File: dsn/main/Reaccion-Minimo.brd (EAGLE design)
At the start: 68.2 x 35.5 mm, 43 parts, among them U1 ATMEGA328P_TQFP, U2 MIC5219 5V, Y1 16MHz

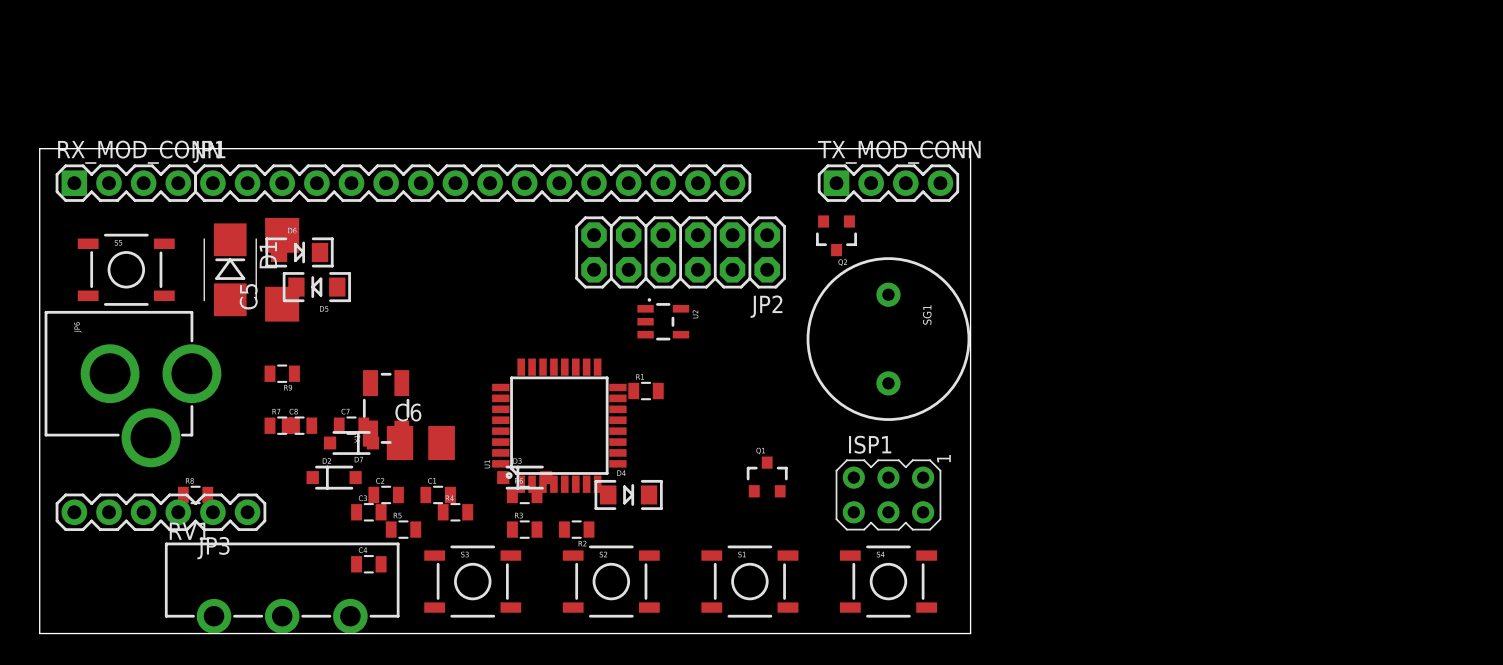
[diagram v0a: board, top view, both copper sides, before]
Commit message: Reaccion Minimo UI finished. RX send tested.
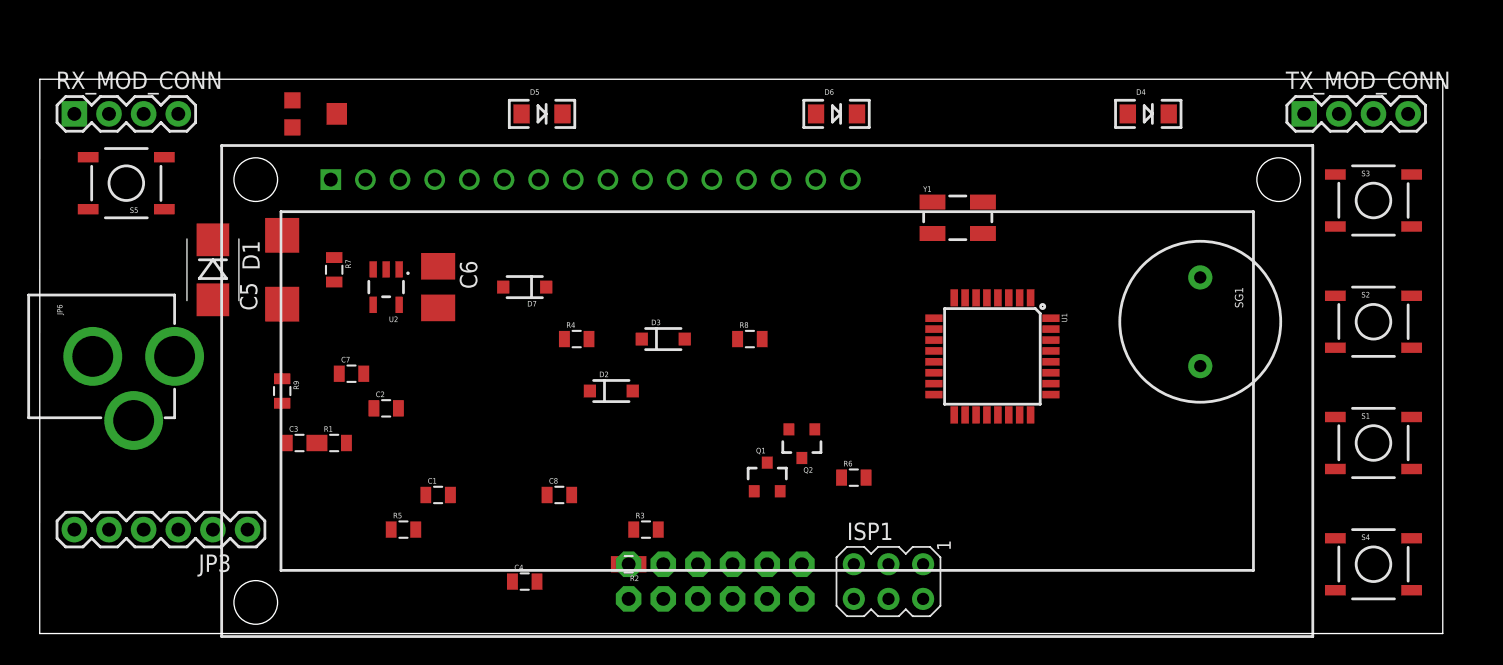
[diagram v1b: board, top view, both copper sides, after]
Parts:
- removed JP1: (no value), SparkFun-Connectors:1X16
- removed RV1: (no value), SparkFun-Electromechanical:POT_ALPHA_RV16AF-20
- added U$1: LCD-HD447803-HOLES16X2-3-HOLES, HD44780LCD:LCD-16X2-3HOLES
- added U$2: TC33, Reaccion-Minimo:TC33
- moved S3 71.7 mm to (97.8, 31.8)
- moved S2 59.0 mm to (97.8, 22.9)
- moved D4 47.2 mm to (81.3, 38.1)
- moved S1 46.8 mm to (97.8, 14.0)
- moved Y1 44.2 mm to (67.3, 30.5), turned to 0 degrees
- moved R8 42.2 mm to (52.1, 21.6)
- moved D6 40.7 mm to (58.4, 38.1)
- moved S4 35.6 mm to (97.8, 5.08)
- moved TX_MOD_CONN 34.7 mm to (92.7, 38.1)
- moved U1 32.2 mm to (69.8, 20.3), turned to 270 degrees
- moved JP2 26.2 mm to (43.2, 5.08), flipped to the bottom
- moved R6 24.2 mm to (59.7, 11.4)
- moved R1 23.2 mm to (21.6, 14.0)
- moved SG1 22.9 mm to (85.1, 22.9)
- moved D2 21.3 mm to (41.9, 17.8)
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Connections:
- net 5V: now also U$1.2, U$2.1; no longer JP1.2, RV1.3
- net D2: now also U$1.11; no longer JP1.11
- net D3: now also U$1.12; no longer JP1.12
- net D4: now also U$1.13; no longer JP1.13
- net D6: now also U$1.14; no longer JP1.14
- net D8: now also U$1.4; no longer JP1.4
- net D9: now also U$1.6; no longer JP1.6
- net GND: now also U$1.1, U$1.5, U$2.3; no longer JP1.1, JP1.5, RV1.1
- net N$6: now also U$1.15; no longer JP1.15
- net N$7: now also U$1.3, U$2.2; no longer JP1.3, RV1.2
- net N$8: now also U$1.16; no longer JP1.16
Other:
- board size 68.2 x 35.5 mm -> 102.9 x 40.6 mm

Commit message: Added Reaccion-Minimo PASTO
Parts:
- removed D4: GREEN, SparkFun-LED:LED-1206
- removed S5: SWITCH-MOMENTARY-2SMD, SparkFun-Electromechanical:TACTILE-SWITCH-SMD
- removed U$1: LCD-HD447803-HOLES16X2-3-HOLES, HD44780LCD:LCD-16X2-3HOLES
- added C9: 1uF, SparkFun-Capacitors:0805
- added LCD: LCD-HD447803-HOLES16X2-3-HOLES, HD44780LCD:LCD-16X2-3HOLES
- added RESET: SWITCH-MOMENTARY-2SMD, SparkFun-Electromechanical:TACTILE-SWITCH-SMD
- added U3: WS2811, SparkFun-LED:LED-TRICOLOR-5050-IC
- C1, C2: value (none) -> 18pF
- C3, C7: value (none) -> 1uF
- C4: value (none) -> 0.1uF
- C6: value (none) -> 100uF
- C8: value (none) -> 4.7uF
- R1, R6, R8: value (none) -> 4.7K
- R2: value (none) -> 150
- R3, R4: value (none) -> 330
- R5: value (none) -> 0
- U2: value MIC5219 5V -> lp2992aim5-5.0
- moved R2 52.7 mm to (85.1, 37.1), turned to 270 degrees
- moved R5 39.5 mm to (54.4, 35.8), turned to 90 degrees
- moved D3 35.0 mm to (12.7, 33.3), turned to 270 degrees
- moved R3 34.4 mm to (31.2, 39.4), turned to 180 degrees
- moved D2 32.2 mm to (73.7, 12.2), turned to 270 degrees
- moved C3 30.5 mm to (49.5, 12.4), turned to 90 degrees
- moved C1 28.8 mm to (57.9, 12.2), turned to 90 degrees
- moved C2 25.9 mm to (50.3, 9.40)
- moved R4 24.8 mm to (56.6, 39.4), turned to 180 degrees
- moved R1 23.5 mm to (10.2, 34.5), turned to 90 degrees
- moved Q1 23.1 mm to (61.0, 33.3), turned to 90 degrees
- moved Y1 22.9 mm to (53.6, 12.2), turned to 180 degrees
- moved C4 21.7 mm to (15.2, 11.4), turned to 90 degrees
- moved R8 21.2 mm to (71.1, 12.2), turned to 270 degrees
- moved R6 19.1 mm to (61.0, 30.5), turned to 180 degrees
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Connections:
- net 5V: now also C9.2, LCD.2, U3.3, U3.5; no longer R2.2, U$1.2
- net D2: now also LCD.11; no longer U$1.11
- net D3: now also LCD.12; no longer U$1.12
- net D4: now also LCD.13; no longer U$1.13
- net D6: now also LCD.14; no longer U$1.14
- net D8: now also LCD.4; no longer U$1.4
- net D9: now also LCD.6; no longer U$1.6
- net GND: now also C9.1, LCD.1, LCD.5, RESET.1, U3.6; no longer S5.1, U$1.1, U$1.5
- net HEARTBEAT: now also R2.2; no longer D4.C
- net N$3: now also U3.2; no longer D4.A
- net N$6: now also LCD.15; no longer U$1.15
- net N$7: now also LCD.3; no longer U$1.3
- net N$8: now also LCD.16; no longer U$1.16
- net RESET: now also RESET.3; no longer S5.3
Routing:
- net GND: track 0.00 -> 364.9 mm, vias 0 -> 14
- net 5V: track 0.00 -> 308.0 mm, vias 0 -> 8
- net VIN_RECT: track 0.00 -> 182.3 mm, vias 0 -> 4
- net RESET: track 0.00 -> 148.3 mm, vias 0 -> 2
- net RF_TX: track 0.00 -> 108.9 mm, vias 0 -> 4
- net RF_RX: track 0.00 -> 99.1 mm, vias 0 -> 4
- net BTN_BUS0: track 0.00 -> 92.4 mm, vias 0 -> 4
- net D8: track 0.00 -> 83.8 mm, vias 0 -> 6
- net BTN_BUS3: track 0.00 -> 79.9 mm, vias 0 -> 4
- net BTN_BUS2: track 0.00 -> 62.1 mm, vias 0 -> 2
- net BTN_BUS1: track 0.00 -> 62.0 mm, vias 0 -> 2
- net D9: track 0.00 -> 59.7 mm, vias 0 -> 4
- net RX: track 0.00 -> 56.8 mm, vias 0 -> 2
- net TX: track 0.00 -> 51.1 mm, vias 0 -> 2
- net ADC6: track 0.00 -> 41.5 mm, vias 0 -> 2
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- added copper zone on layer 1, net GND
- added copper zone on layer 16, net GND
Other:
- board size 102.9 x 40.6 mm -> 102.9 x 44.5 mm
- board text added: "Galeras volcano. Artwork generated from Jorge Luis Recalde Mesías photo CC BY-SA 3.0"
- board text added: "Reaccion-Minimo Codename Colibri Designed in El Salvador Made in Colombia Version 0.1 10/16"
